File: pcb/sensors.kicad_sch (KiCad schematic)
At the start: 19 parts, among them J2 Conn_01x04, J3 Conn_01x04, U3 BME280, U4 SGP41, U6 SN65HVD485EDR, U7 2N7001TDPWR, U8 2N7001TDPWR, U9 2N7001TDPWR

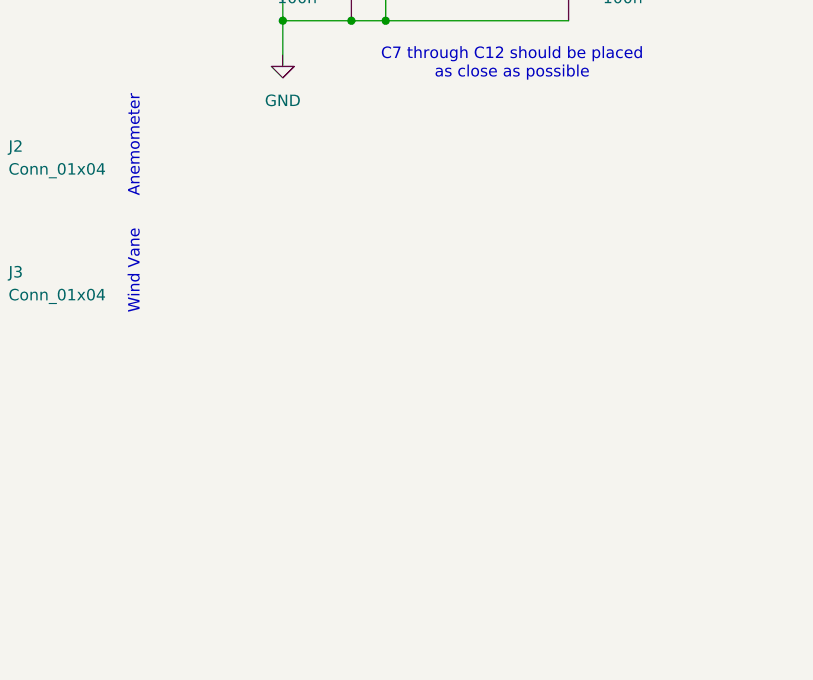
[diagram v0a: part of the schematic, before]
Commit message: feat: RJ11 connector, partial BOM fulfillment
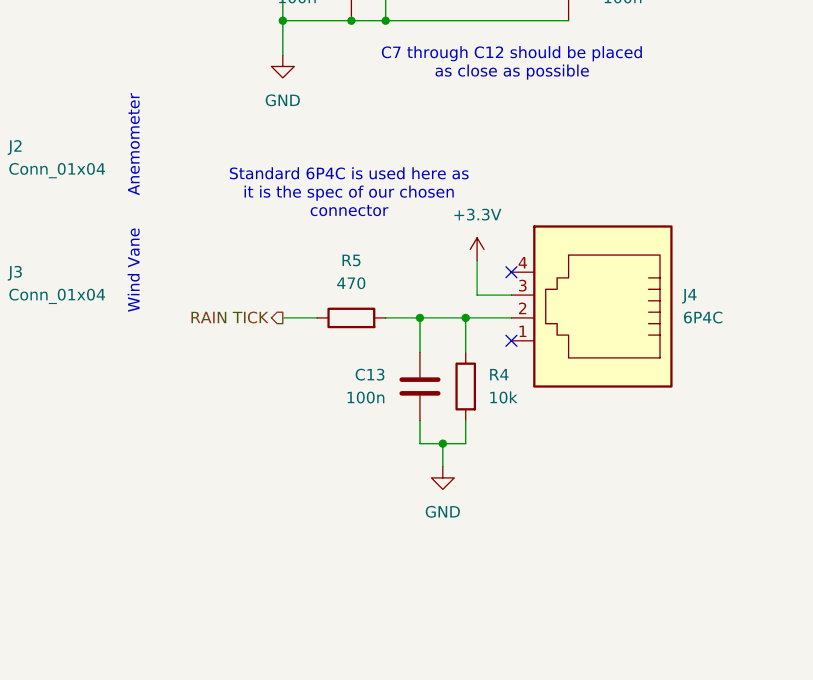
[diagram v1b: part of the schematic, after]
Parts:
- added C13: 100n, symbol Device:C
- added J4: 6P4C, Banshee:5501-4P4C-13MM, symbol Connector:6P4C
- added R4: 10k, symbol Device:R
- added R5: 470, symbol Device:R
- J2, J3: now left out of the parts list
- U3: JLCPCB Part# (none) -> C92489
- U4: JLCPCB Part# (none) -> C3659325
- U6: JLCPCB Part# (none) -> C27899
- U7, U8, U9: JLCPCB Part# (none) -> C2652968
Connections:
- net +3.3V: now also J4.3
- net GND: now also C13.2, R4.2
- new net: C13.1, J4.2, R4.1, R5.2
- new net RAIN TICK: R5.1
- no-connect marks 0 -> 2
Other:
- note added: "Standard 6P4C is used here as it is the spec of our chosen connector"

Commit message: chore: finalized rain gauge sensor thingymajig
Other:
- note added: "Rain Gauge: Connector"
- moved on the sheet: C13, J2, J3, J4, R4, R5

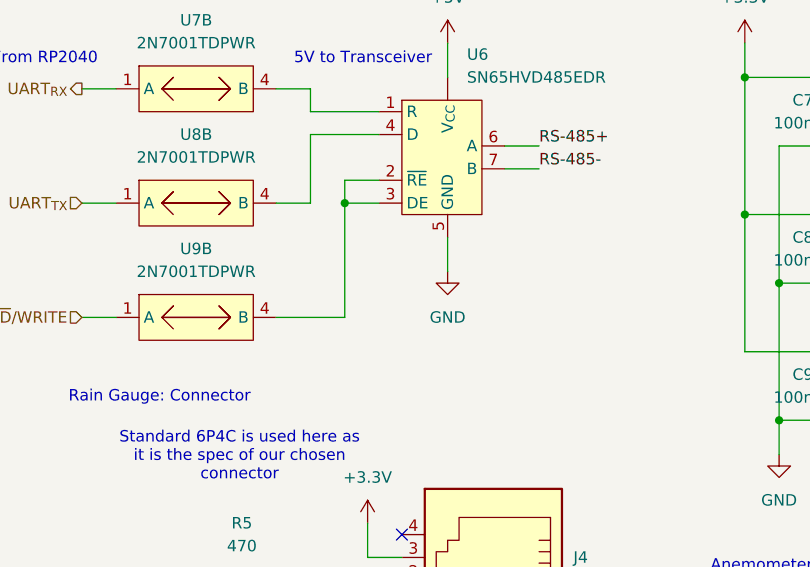
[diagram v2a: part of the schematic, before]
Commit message: chore: added pull-down on rs-485 transceiver
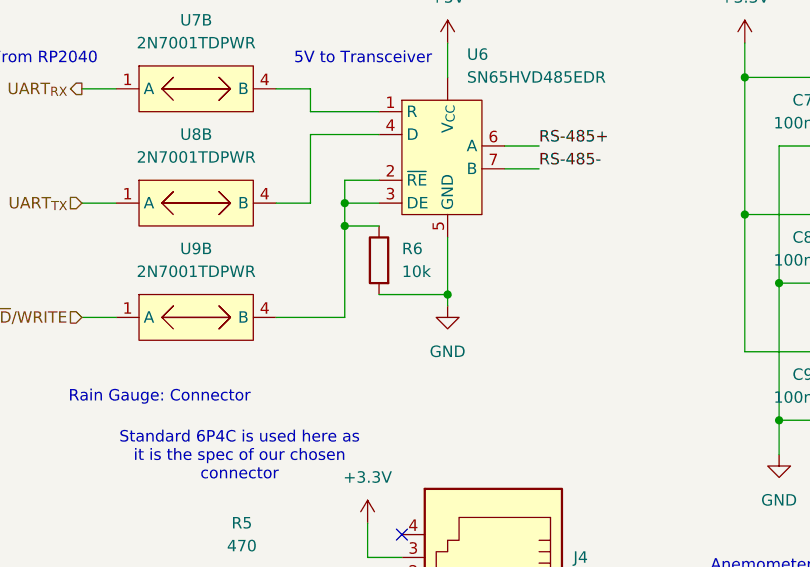
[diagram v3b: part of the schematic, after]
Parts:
- added R6: 10k, symbol Device:R
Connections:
- net GND: now also R6.2
- net at U6.2 (~{RE}), U6.3 (DE), U9.4 (B): now also R6.1
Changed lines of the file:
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@@
 	)
 	(junction
+		(at 184.15 45.72)
+		(diameter 0)
+		(color 0 0 0 0)
+	)
+	(junction
 		(at 182.88 99.06)
 		(diameter 0)
@@
 	)
 	(junction
+		(at 195.58 53.34)
+		(diameter 0)
+		(color 0 0 0 0)
+	)
+	(junction
 		(at 66.04 121.92)
 		(diameter 0)
@@
 	(wire
 		(pts
+			(xy 184.15 45.72) (xy 184.15 43.18)
+		)
+		(stroke
+			(width 0)
+			(type default)
+		)
+	)
+	(wire
+		(pts
 			(xy 245.11 99.06) (xy 254 99.06)
 		)
@@
 	(wire
 		(pts
-			(xy 184.15 55.88) (xy 184.15 43.18)
+			(xy 184.15 55.88) (xy 184.15 45.72)
 		)
 		(stroke
@@
 	(wire
 		(pts
-			(xy 195.58 46.99) (xy 195.58 50.8)
+			(xy 195.58 53.34) (xy 195.58 54.61)
+		)
+		(stroke
+			(width 0)
+			(type default)
+		)
+	)
+	(wire
+		(pts
+			(xy 195.58 46.99) (xy 195.58 53.34)
 		)
 		(stroke
@@
 	(wire
 		(pts
+			(xy 187.96 53.34) (xy 195.58 53.34)
+		)
+		(stroke
+			(width 0)
+			(type default)
+		)
+	)
+	(wire
+		(pts
 			(xy 243.84 31.75) (xy 243.84 36.83)
 		)
@@
 	(wire
 		(pts
+			(xy 184.15 45.72) (xy 187.96 45.72)
+		)
+		(stroke
+			(width 0)
+			(type default)
+		)
+	)
+	(wire
+		(pts
 			(xy 154.94 55.88) (xy 158.75 55.88)
 		)
@@
 	)
 	(symbol
+		(lib_id "Device:R")
+		(at 187.96 49.53 0)
+		(mirror y)
+		(unit 1)
+		(exclude_from_sim no)
+		(in_bom yes)
+		(on_board yes)
+		(dnp no)
+		(property "Reference" "R6"
+			(at 190.5 48.2599 0)
+			(effects
+				(font
+					(size 1.27 1.27)
+				)
+				(justify right)
+			)
+		)
+		(property "Value" "10k"
+			(at 190.5 50.7999 0)
+			(effects
+				(font
+					(size 1.27 1.27)
+				)
+				(justify right)
+			)
+		)
+		(property "Footprint" ""
+			(at 189.738 49.53 90)
+			(effects
+				(font
+					(size 1.27 1.27)
+				)
+				(hide yes)
+			)
+		)
+		(property "Datasheet" "~"
+			(at 187.96 49.53 0)
+			(effects
+				(font
+					(size 1.27 1.27)
+				)
+				(hide yes)
+			)
+		)
+		(property "Description" "Resistor"
+			(at 187.96 49.53 0)
+			(effects
+				(font
+					(size 1.27 1.27)
+				)
+				(hide yes)
+			)
+		)
+		(property "JLCPCB Part#" ""
+			(at 187.96 49.53 0)
+			(effects
+				(font
+					(size 1.27 1.27)
+				)
+				(hide yes)
+			)
+		)
+		(pin "1"
+		)
+		(pin "2"
+		)
+		(instances
+			(project "pcb"
+				(path "/9bba97c2-2e09-46fb-bf2a-7de104403c7c/0b6630c6-ecdb-4ee5-ae06-53316b49d000"
+					(reference "R6")
+					(unit 1)
+				)
+			)
+		)
+	)
+	(symbol
 		(lib_id "Device:C")
 		(at 58.42 34.29 0)
@@
 	(symbol
 		(lib_id "power:GND")
-		(at 195.58 50.8 0)
+		(at 195.58 54.61 0)
 		(unit 1)
 		(exclude_from_sim no)
@@
 		(fields_autoplaced yes)
 		(property "Reference" "#PWR018"
-			(at 195.58 57.15 0)
+			(at 195.58 60.96 0)
 			(effects
 				(font
@@
 		)
 		(property "Value" "GND"
-			(at 195.58 55.88 0)
+			(at 195.58 59.69 0)
 			(effects
 				(font
@@
 		)
 		(property "Footprint" ""
-			(at 195.58 50.8 0)
+			(at 195.58 54.61 0)
 			(effects
 				(font
@@
 		)
 		(property "Datasheet" ""
-			(at 195.58 50.8 0)
+			(at 195.58 54.61 0)
 			(effects
 				(font
@@
 		)
 		(property "Description" "Power symbol creates a global label with name \"GND\" , ground"
-			(at 195.58 50.8 0)
+			(at 195.58 54.61 0)
 			(effects
 				(font

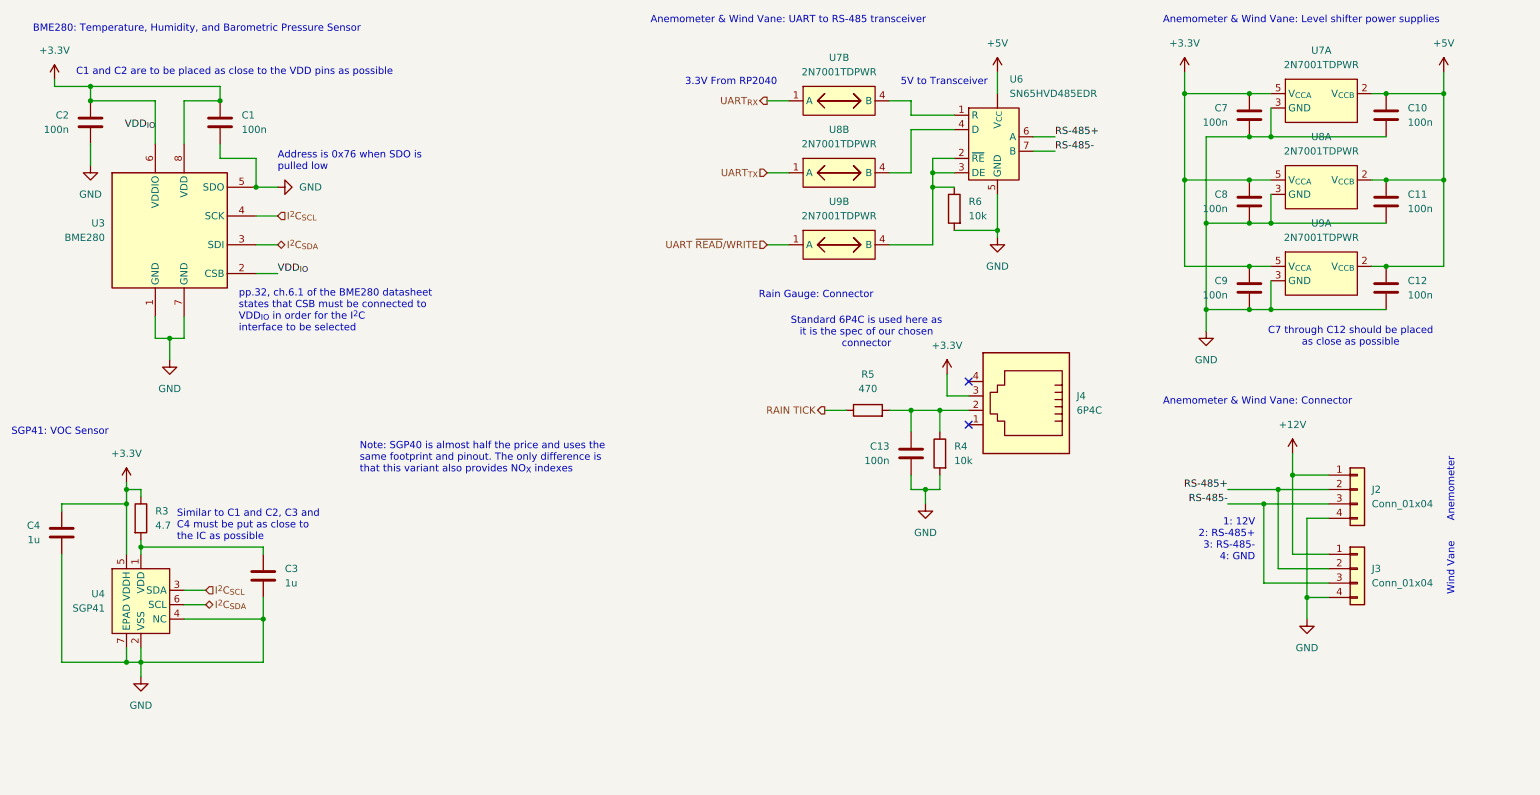
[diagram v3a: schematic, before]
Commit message: feat: PMS7003 sensor
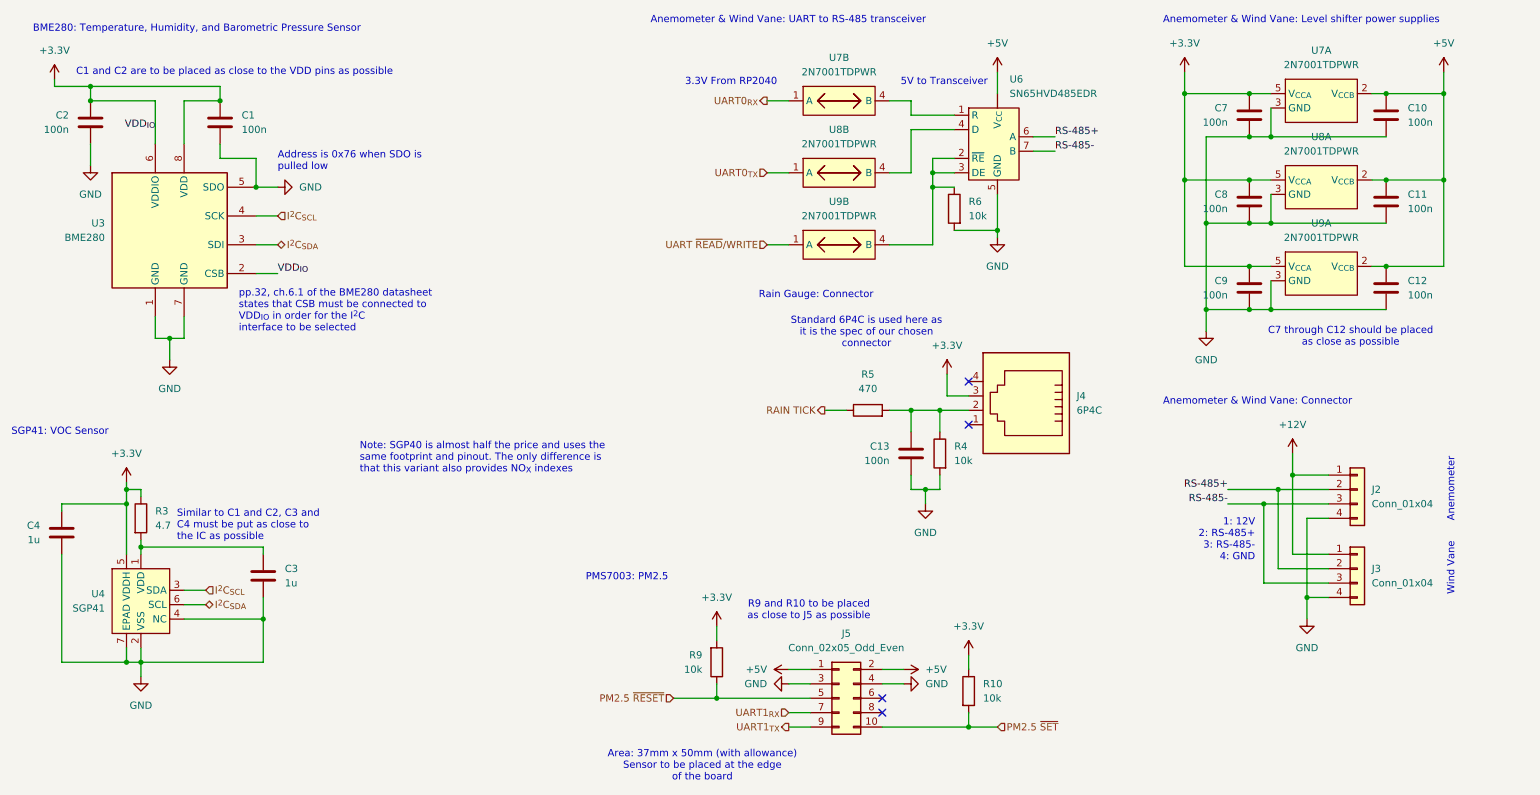
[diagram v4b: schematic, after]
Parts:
- added J5: Conn_02x05_Odd_Even, symbol Connector_Generic:Conn_02x05_Odd_Even
- added R10, R9: 10k, symbol Device:R
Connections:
- net +3.3V: now also R10.1, R9.2
- net +5V: now also J5.1 (Pin_1), J5.2 (Pin_2)
- net GND: now also J5.3 (Pin_3), J5.4 (Pin_4)
- net UART_{RX} renamed UART0_{RX}
- net UART_{TX} renamed UART0_{TX}
- new net PM2.5 ~{RESET}: J5.5 (Pin_5), R9.1
- new net PM2.5 ~{SET}: J5.10 (Pin_10), R10.2
- new net UART1_{RX}: J5.7 (Pin_7)
- new net UART1_{TX}: J5.9 (Pin_9)
- no-connect marks 2 -> 4
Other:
- note added: "Area: 37mm x 50mm (with allowance) Sensor to be placed at the edge of the board"
- note added: "PMS7003: PM2.5"
- note added: "R9 and R10 to be placed as close to J5 as possible"

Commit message: feat: finalized usb receptacle
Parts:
- J2, J3: footprint (none) -> Connector_PinHeader_2.54mm:PinHeader_1x04_P2.54mm_Vertical
- J5: footprint (none) -> Connector_PinHeader_1.27mm:PinHeader_2x05_P1.27mm_Vertical
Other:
- note added: "Area: 48mm x 37mm Sensor to be placed at the edge of the board"
- note removed: "Area: 37mm x 50mm (with allowance) Sensor to be placed at the edge of the board"
- moved on the sheet: C13, J4, J5, R10, R4, R5, R6, R9, U6, U7B, U8B, U9B

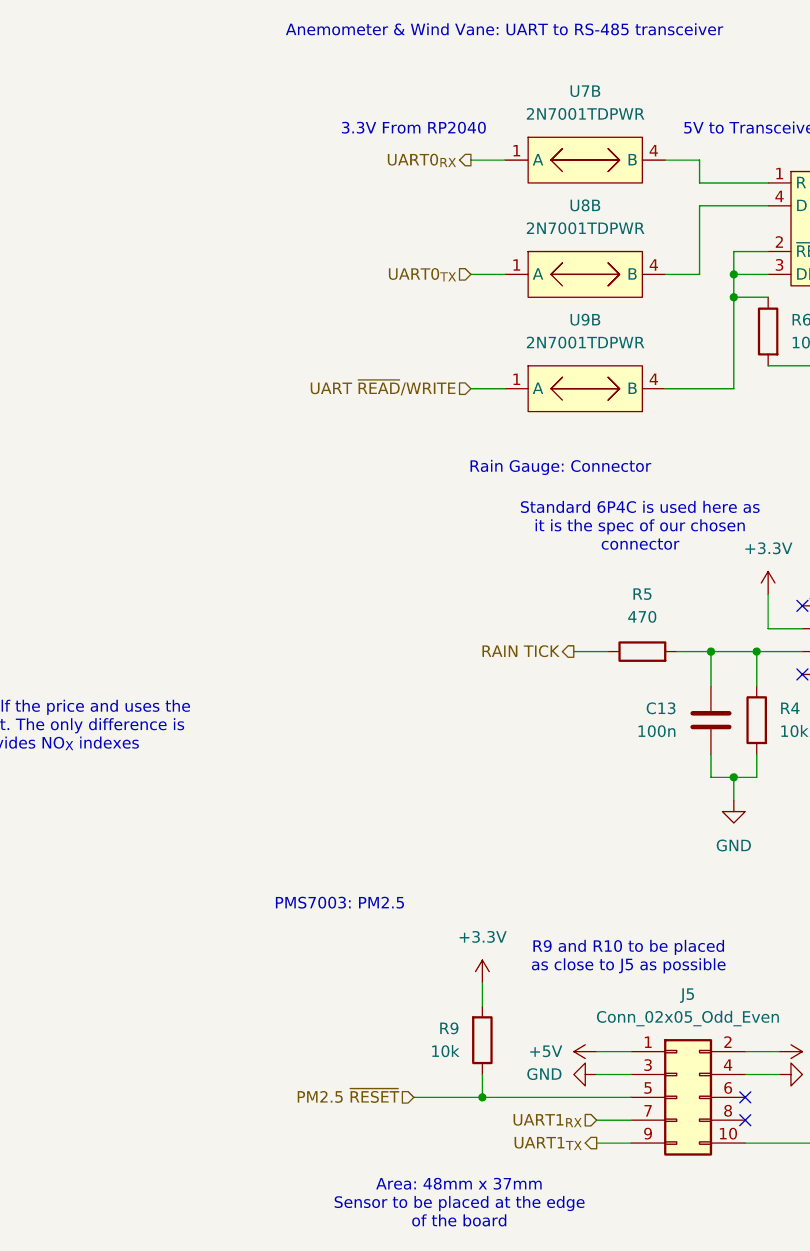
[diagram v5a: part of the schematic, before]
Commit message: feat: reserved connections for SX1278 lora module
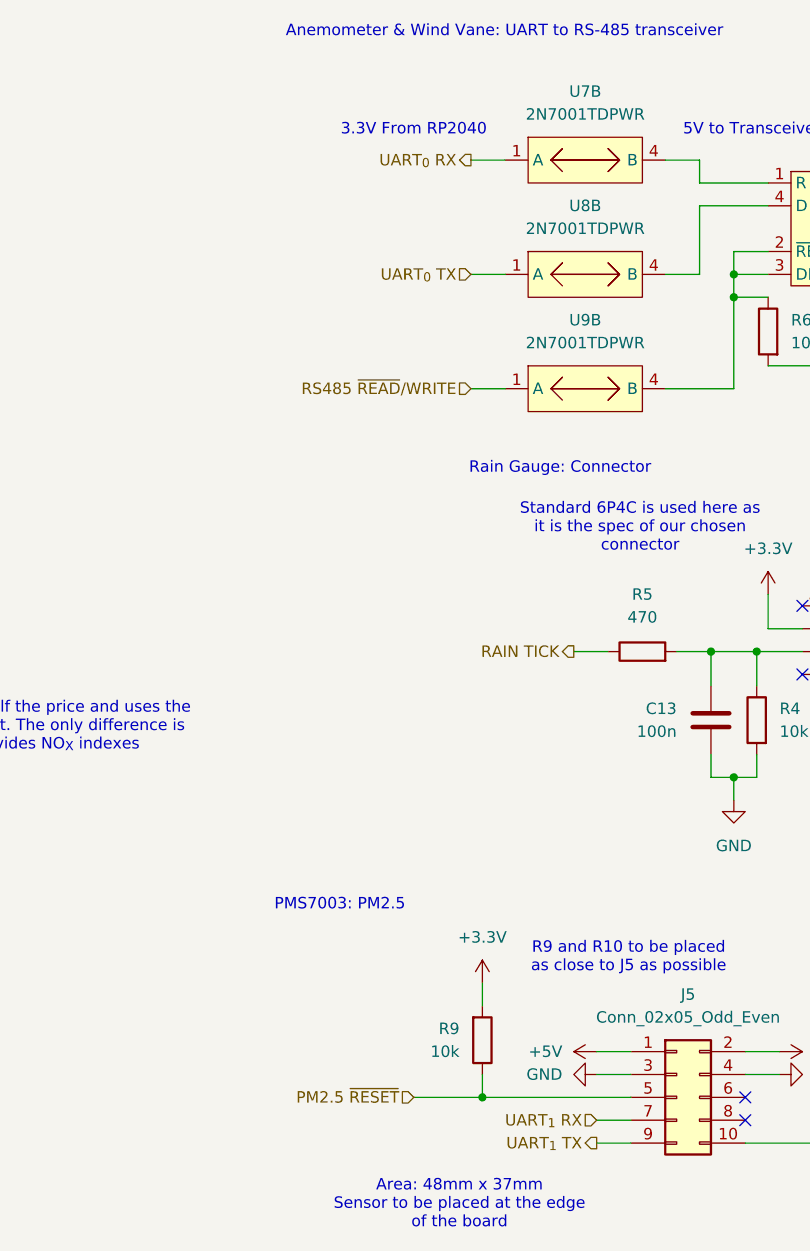
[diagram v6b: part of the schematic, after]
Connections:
- net UART ~{READ}/WRITE renamed RS485 ~{READ}/WRITE
- net UART0_{RX} renamed UART_{0} RX
- net UART0_{TX} renamed UART_{0} TX
- net UART1_{RX} renamed UART_{1} RX
- net UART1_{TX} renamed UART_{1} TX
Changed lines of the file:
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@@
 		)
 	)
-	(hierarchical_label "UART1_{RX}"
+	(hierarchical_label "UART_{1} RX"
 		(shape input)
 		(at 171.45 137.16 180)
@@
 		)
 	)
-	(hierarchical_label "UART ~{READ}{slash}WRITE"
+	(hierarchical_label "RS485 ~{READ}{slash}WRITE"
 		(shape input)
 		(at 157.48 55.88 180)
@@
 		)
 	)
-	(hierarchical_label "UART1_{TX}"
+	(hierarchical_label "UART_{1} TX"
 		(shape output)
 		(at 171.45 139.7 180)
@@
 		)
 	)
-	(hierarchical_label "UART0_{TX}"
+	(hierarchical_label "UART_{0} TX"
 		(shape input)
 		(at 157.48 43.18 180)
@@
 		)
 	)
-	(hierarchical_label "UART0_{RX}"
+	(hierarchical_label "UART_{0} RX"
 		(shape output)
 		(at 157.48 30.48 180)

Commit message: chore: date update
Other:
- title: Banshee Sensor Array -> Banshee Microcontroller + Supporting Systems
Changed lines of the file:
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@@
 	(paper "A4")
 	(title_block
-		(title "Banshee Sensor Array")
-		(date "2026-01-29")
+		(title "Banshee Microcontroller + Supporting Systems")
+		(date "2026-02-05")
 		(rev "1")
 		(company "Ivan Leonard O Aparte <ivanleonard.aparte@cit.edu>")
